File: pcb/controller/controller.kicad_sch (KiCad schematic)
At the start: 1 part, among them U1 XIAO-ESP32-S3-SMD

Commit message: cleaned up
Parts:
- U1: value XIAO-ESP32-S3-SMD -> XIAO-ESP32-C6-SMD
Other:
- note removed: "Target interface"
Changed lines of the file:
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@@
 	(generator_version "9.0")
 	(paper "A4")
-	(text "Target interface"
-		(exclude_from_sim no)
-		(at 248.158 15.24 0)
-		(effects
-			(font
-				(size 1.27 1.27)
-			)
-		)
-	)
 	(no_connect
 		(at 107.95 119.38)
@@
 			)
 		)
-		(property "Value" "XIAO-ESP32-S3-SMD"
+		(property "Value" "XIAO-ESP32-C6-SMD"
 			(at 110.0933 121.92 0)
 			(effects

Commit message: implemented PD, buck and LDO for Power Input
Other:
- sheet Power Input ports: added none; removed GND
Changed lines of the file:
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@@
-	(wire
-		(pts
-			(xy 39.37 43.18) (xy 39.37 45.72)
-		)
-		(stroke
-			(width 0)
-			(type default)
-		)
-	)
 	(wire
 		(pts
@@
 	(wire
 		(pts
-			(xy 39.37 67.31) (xy 39.37 71.12)
-		)
-		(stroke
-			(width 0)
-			(type default)
-		)
-	)
-	(wire
-		(pts
 			(xy 59.69 86.36) (xy 83.82 86.36)
 		)
@@
 		(pts
 			(xy 63.5 99.06) (xy 63.5 90.17)
+		)
+		(stroke
+			(width 0)
+			(type default)
+		)
+	)
+	(wire
+		(pts
+			(xy 41.91 48.26) (xy 41.91 50.8)
 		)
 		(stroke
@@
 	(symbol
 		(lib_id "power:GND")
-		(at 39.37 71.12 0)
-		(unit 1)
-		(exclude_from_sim no)
-		(in_bom yes)
-		(on_board yes)
-		(dnp no)
-		(fields_autoplaced yes)
-		(property "Reference" "#PWR02"
-			(at 39.37 77.47 0)
-			(effects
-				(font
-					(size 1.27 1.27)
-				)
-				(hide yes)
-			)
-		)
-		(property "Value" "GND"
-			(at 39.37 76.2 0)
-			(effects
-				(font
-					(size 1.27 1.27)
-				)
-			)
-		)
-		(property "Footprint" ""
-			(at 39.37 71.12 0)
-			(effects
-				(font
-					(size 1.27 1.27)
-				)
-				(hide yes)
-			)
-		)
-		(property "Datasheet" ""
-			(at 39.37 71.12 0)
-			(effects
-				(font
-					(size 1.27 1.27)
-				)
-				(hide yes)
-			)
-		)
-		(property "Description" "Power symbol creates a global label with name \"GND\" , ground"
-			(at 39.37 71.12 0)
-			(effects
-				(font
-					(size 1.27 1.27)
-				)
-				(hide yes)
-			)
-		)
-		(pin "1"
-		)
-		(instances
-			(project ""
-				(path "/c599d8cf-7937-49be-b4ed-eac09167ead4"
-					(reference "#PWR02")
-					(unit 1)
-				)
-			)
-		)
-	)
-	(symbol
-		(lib_id "power:GND")
 		(at 140.97 90.17 0)
 		(unit 1)
@@
 	(symbol
 		(lib_id "power:+5V")
-		(at 39.37 43.18 0)
+		(at 41.91 48.26 0)
 		(unit 1)
 		(exclude_from_sim no)
@@
 		(fields_autoplaced yes)
 		(property "Reference" "#PWR01"
-			(at 39.37 46.99 0)
+			(at 41.91 52.07 0)
 			(effects
 				(font
@@
 		)
 		(property "Value" "+5V"
-			(at 39.37 38.1 0)
+			(at 41.91 43.18 0)
 			(effects
 				(font
@@
 		)
 		(property "Footprint" ""
-			(at 39.37 43.18 0)
+			(at 41.91 48.26 0)
 			(effects
 				(font
@@
 		)
 		(property "Datasheet" ""
-			(at 39.37 43.18 0)
+			(at 41.91 48.26 0)
 			(effects
 				(font
@@
 		)
 		(property "Description" "Power symbol creates a global label with name \"+5V\""
-			(at 39.37 43.18 0)
+			(at 41.91 48.26 0)
 			(effects
 				(font
@@
 	)
 	(sheet
-		(at 25.4 45.72)
-		(size 26.67 21.59)
+		(at 27.94 50.8)
+		(size 27.94 5.08)
 		(exclude_from_sim no)
 		(in_bom yes)
@@
 		)
 		(property "Sheetname" "Power Input"
-			(at 25.4 45.0084 0)
+			(at 27.94 50.0884 0)
 			(effects
 				(font
@@
 		)
 		(property "Sheetfile" "power_input.kicad_sch"
-			(at 25.4 67.8946 0)
+			(at 27.94 56.4646 0)
 			(effects
 				(font
@@
 			)
 		)
-		(pin "GND" output
-			(at 39.37 67.31 270)
-			(effects
-				(font
-					(size 1.27 1.27)
-				)
-				(justify left)
-			)
-		)
 		(pin "+5V" output
-			(at 39.37 45.72 90)
-			(effects
-				(font
+			(at 41.91 50.8 90)
+			(effects
+				(font

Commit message: impl eFuse
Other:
- sheet Power Input ports: added Imon; removed none
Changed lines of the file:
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@@
+			)
+		)
+		(pin "Imon" output
+			(at 55.88 53.34 0)
+			(effects
+				(font
+					(size 1.27 1.27)
+				)
+				(justify right)
 			)
 		)

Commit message: retraced target pcb
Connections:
- net GND: now also U1.16 (GND), U1.20 (GND)
- net Inputs/RE_B: now also U1.10 (GPIO20_D9_MISO); no longer U1.4 (GPIO21_D3)
- net Inputs/SW1: now also U1.2 (GPIO1_A1_D1); no longer U1.1 (GPIO0_A0_D0)
- net Inputs/SW2: now also U1.3 (GPIO2_A2_D2); no longer U1.2 (GPIO1_A1_D1)
- net Inputs/SW3: now also U1.4 (GPIO21_D3); no longer U1.3 (GPIO2_A2_D2)
- new net Imon: U1.1 (GPIO0_A0_D0)
- no-connect marks 14 -> 11

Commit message: added lcsc numbers to all components and added ESD protection
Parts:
- U1: footprint (none) -> Seeed Studio XIAO Series Library:XIAO-ESP32C6-SMD; now left out of the parts list
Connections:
- net +3.3V: now also U1.24 (3V3_1)
- net Inputs/SW4: now reaches U1.9 (GPIO19_D8_SCK)
- no-connect marks 11 -> 9
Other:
- sheet Inputs ports: added SW4; removed none
- sheet Power Input ports: added none; removed +5V
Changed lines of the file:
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@@
 	(paper "A4")
 	(no_connect
-		(at 119.38 74.93)
-	)
-	(no_connect
-		(at 101.6 119.38)
+		(at 102.87 119.38)
 	)
 	(no_connect
@@
 	)
 	(no_connect
-		(at 127 105.41)
-	)
-	(no_connect
 		(at 92.71 74.93)
 	)
@@
 	(wire
 		(pts
+			(xy 130.81 132.08) (xy 130.81 105.41)
+		)
+		(stroke
+			(width 0)
+			(type default)
+		)
+	)
+	(wire
+		(pts
 			(xy 69.85 99.06) (xy 49.53 99.06)
 		)
@@
 	(wire
 		(pts
-			(xy 137.16 128.27) (xy 69.85 128.27)
-		)
-		(stroke
-			(width 0)
-			(type default)
-		)
-	)
-	(wire
-		(pts
-			(xy 137.16 97.79) (xy 137.16 128.27)
+			(xy 137.16 137.16) (xy 68.58 137.16)
+		)
+		(stroke
+			(width 0)
+			(type default)
+		)
+	)
+	(wire
+		(pts
+			(xy 119.38 72.39) (xy 119.38 74.93)
+		)
+		(stroke
+			(width 0)
+			(type default)
+		)
+	)
+	(wire
+		(pts
+			(xy 73.66 111.76) (xy 73.66 132.08)
+		)
+		(stroke
+			(width 0)
+			(type default)
+		)
+	)
+	(wire
+		(pts
+			(xy 137.16 97.79) (xy 137.16 137.16)
 		)
 		(stroke
@@
 	(wire
 		(pts
-			(xy 49.53 106.68) (xy 72.39 106.68)
-		)
-		(stroke
-			(width 0)
-			(type default)
-		)
-	)
-	(wire
-		(pts
-			(xy 69.85 128.27) (xy 69.85 110.49)
+			(xy 49.53 115.57) (xy 71.12 115.57)
+		)
+		(stroke
+			(width 0)
+			(type default)
+		)
+	)
+	(wire
+		(pts
+			(xy 68.58 137.16) (xy 68.58 119.38)
 		)
 		(stroke
@@
 	(wire
 		(pts
-			(xy 72.39 106.68) (xy 72.39 125.73)
-		)
-		(stroke
-			(width 0)
-			(type default)
-		)
-	)
-	(wire
-		(pts
-			(xy 72.39 125.73) (xy 133.35 125.73)
+			(xy 49.53 111.76) (xy 73.66 111.76)
+		)
+		(stroke
+			(width 0)
+			(type default)
+		)
+	)
+	(wire
+		(pts
+			(xy 71.12 115.57) (xy 71.12 134.62)
+		)
+		(stroke
+			(width 0)
+			(type default)
+		)
+	)
+	(wire
+		(pts
+			(xy 71.12 134.62) (xy 133.35 134.62)
+		)
+		(stroke
+			(width 0)
+			(type default)
+		)
+	)
+	(wire
+		(pts
+			(xy 127 105.41) (xy 130.81 105.41)
 		)
 		(stroke
@@
 	(wire
 		(pts
-			(xy 69.85 110.49) (xy 49.53 110.49)
+			(xy 68.58 119.38) (xy 49.53 119.38)
 		)
 		(stroke
@@
 	(wire
 		(pts
-			(xy 41.91 48.26) (xy 41.91 50.8)
-		)
-		(stroke
-			(width 0)
-			(type default)
-		)
-	)
-	(wire
-		(pts
 			(xy 67.31 90.17) (xy 83.82 90.17)
 		)
@@
 	(wire
 		(pts
-			(xy 133.35 125.73) (xy 133.35 101.6)
+			(xy 73.66 132.08) (xy 130.81 132.08)
+		)
+		(stroke
+			(width 0)
+			(type default)
+		)
+	)
+	(wire
+		(pts
+			(xy 133.35 134.62) (xy 133.35 101.6)
 		)
 		(stroke
@@
 		(unit 1)
 		(exclude_from_sim no)
-		(in_bom yes)
+		(in_bom no)
 		(on_board yes)
 		(dnp no)
@@
 			)
 		)
-		(property "Footprint" ""
+		(property "Footprint" "Seeed Studio XIAO Series Library:XIAO-ESP32C6-SMD"
 			(at 96.52 92.71 0)
 			(effects
@@
 		)
 		(property "Description" ""
+			(at 105.41 97.79 0)
+			(effects
+				(font
+					(size 1.27 1.27)
+				)
+				(hide yes)
+			)
+		)
+		(property "LCSC" ""
 			(at 105.41 97.79 0)
 			(effects
@@
 	)
 	(symbol
-		(lib_id "power:+5V")
-		(at 41.91 48.26 0)
+		(lib_id "power:+3.3V")
+		(at 119.38 72.39 0)
 		(unit 1)
 		(exclude_from_sim no)
@@
 		(on_board yes)
 		(dnp no)
-		(fields_autoplaced yes)
 		(property "Reference" "#PWR01"
-			(at 41.91 52.07 0)
-			(effects
-				(font
-					(size 1.27 1.27)
-				)
-				(hide yes)
-			)
-		)
-		(property "Value" "+5V"
-			(at 41.91 43.18 0)
+			(at 119.38 76.2 0)
+			(effects
+				(font
+					(size 1.27 1.27)
+				)
+				(hide yes)
+			)
+		)
+		(property "Value" "+3.3V"
+			(at 123.444 71.12 0)
 			(effects
 				(font
@@
 		)
 		(property "Footprint" ""
-			(at 41.91 48.26 0)
+			(at 119.38 72.39 0)
 			(effects
 				(font
@@
 		)
 		(property "Datasheet" ""
-			(at 41.91 48.26 0)
-			(effects
-				(font
-					(size 1.27 1.27)
-				)
-				(hide yes)
-			)
-		)
-		(property "Description" "Power symbol creates a global label with name \"+5V\""
-			(at 41.91 48.26 0)
+			(at 119.38 72.39 0)
+			(effects
+				(font
+					(size 1.27 1.27)
+				)
+				(hide yes)
+			)
+		)
+		(property "Description" "Power symbol creates a global label with name \"+3.3V\""
+			(at 119.38 72.39 0)
 			(effects
 				(font
@@
 		)
 		(instances
-			(project ""
+			(project "controller"
 				(path "/c599d8cf-7937-49be-b4ed-eac09167ead4"
 					(reference "#PWR01")
@@
 			)
 		)
-		(pin "+5V" output
-			(at 41.91 50.8 90)
-			(effects
-				(font
-					(size 1.27 1.27)
-				)
-				(justify right)
-			)
-		)
 		(pin "Imon" output
 			(at 55.88 53.34 0)
@@
 	(sheet
 		(at 25.4 93.98)
-		(size 24.13 19.05)
+		(size 24.13 26.67)
 		(exclude_from_sim no)
 		(in_bom yes)
@@
 		)
 		(property "Sheetfile" "inputs.kicad_sch"
-			(at 25.4 113.6146 0)
+			(at 25.4 121.2346 0)
 			(effects
 				(font
@@
 		)
 		(pin "RE_B" output
-			(at 49.53 106.68 0)
+			(at 49.53 115.57 0)
+			(effects
+				(font
+					(size 1.27 1.27)
+				)
+				(justify right)
+			)
+		)
+		(pin "RE_A" output
+			(at 49.53 119.38 0)
+			(effects
+				(font
+					(size 1.27 1.27)
+				)
+				(justify right)
+			)
+		)
+		(pin "SW2" output
+			(at 49.53 99.06 0)
 			(effects
 				(font
@@
 			)
 		)
-		(pin "RE_A" output
-			(at 49.53 110.49 0)
-			(effects
-				(font
-					(size 1.27 1.27)
-				)
-				(justify right)
-			)
-		)
-		(pin "SW2" output
-			(at 49.53 99.06 0)
-			(effects
-				(font
+		(pin "SW4" output
+			(at 49.53 111.76 0)
+			(effects
+				(font

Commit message: did led circle pcb and added 3d models for the controller pcb
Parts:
- U1: footprint Seeed Studio XIAO Series Library:XIAO-ESP32C6-SMD -> external_footprints.petty:XIAO-ESP32C6-SMD
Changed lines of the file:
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@@
 			)
 		)
-		(property "Footprint" "Seeed Studio XIAO Series Library:XIAO-ESP32C6-SMD"
+		(property "Footprint" "external_footprints.petty:XIAO-ESP32C6-SMD"
 			(at 96.52 92.71 0)
 			(effects

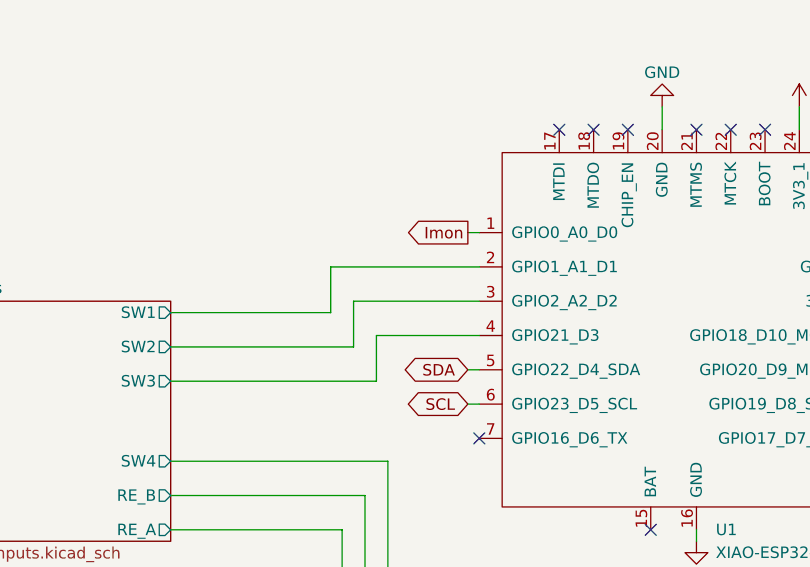
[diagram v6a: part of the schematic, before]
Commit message: traced controller pcb and renamed to Blitzpong
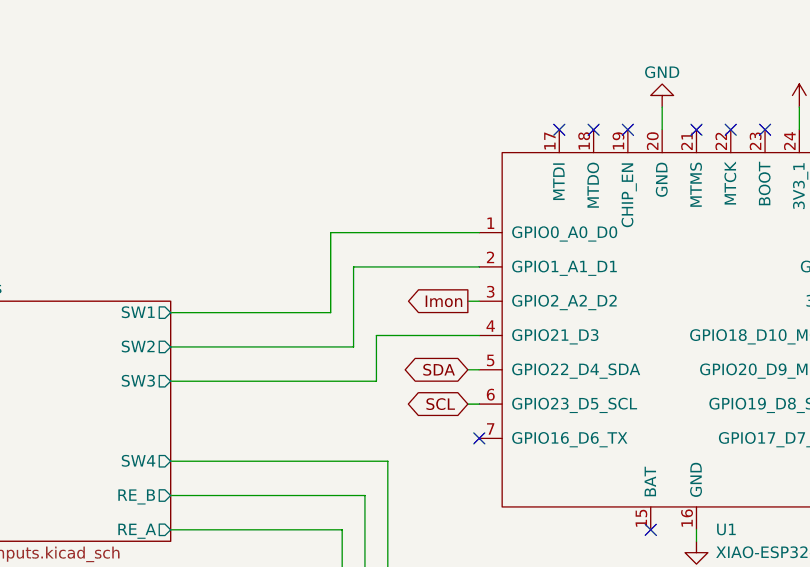
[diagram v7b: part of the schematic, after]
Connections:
- net Imon: now also U1.3 (GPIO2_A2_D2); no longer U1.1 (GPIO0_A0_D0)
- net Inputs/SW1: now also U1.1 (GPIO0_A0_D0); no longer U1.2 (GPIO1_A1_D1)
- net Inputs/SW2: now also U1.2 (GPIO1_A1_D1); no longer U1.3 (GPIO2_A2_D2)
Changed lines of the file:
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@@
+	(wire
+		(pts
+			(xy 82.55 93.98) (xy 83.82 93.98)
+		)
+		(stroke
+			(width 0)
+			(type default)
+		)
+	)
 	(wire
 		(pts
@@
 	(wire
 		(pts
-			(xy 82.55 86.36) (xy 83.82 86.36)
-		)
-		(stroke
-			(width 0)
-			(type default)
-		)
-	)
-	(wire
-		(pts
 			(xy 208.28 85.09) (xy 208.28 88.9)
 		)
@@
 	(wire
 		(pts
-			(xy 69.85 93.98) (xy 69.85 99.06)
-		)
-		(stroke
-			(width 0)
-			(type default)
-		)
-	)
-	(wire
-		(pts
 			(xy 127 101.6) (xy 133.35 101.6)
 		)
@@
 	(wire
 		(pts
-			(xy 67.31 95.25) (xy 67.31 90.17)
+			(xy 67.31 86.36) (xy 67.31 95.25)
 		)
 		(stroke
@@
 	(wire
 		(pts
+			(xy 67.31 86.36) (xy 83.82 86.36)
+		)
+		(stroke
+			(width 0)
+			(type default)
+		)
+	)
+	(wire
+		(pts
 			(xy 82.55 101.6) (xy 83.82 101.6)
 		)
@@
 	(wire
 		(pts
+			(xy 83.82 90.17) (xy 69.85 90.17)
+		)
+		(stroke
+			(width 0)
+			(type default)
+		)
+	)
+	(wire
+		(pts
 			(xy 68.58 119.38) (xy 49.53 119.38)
 		)
@@
 	(wire
 		(pts
-			(xy 83.82 93.98) (xy 69.85 93.98)
-		)
-		(stroke
-			(width 0)
-			(type default)
-		)
-	)
-	(wire
-		(pts
 			(xy 127 97.79) (xy 137.16 97.79)
 		)
@@
 	(wire
 		(pts
-			(xy 67.31 90.17) (xy 83.82 90.17)
+			(xy 69.85 90.17) (xy 69.85 99.06)
 		)
 		(stroke
@@
 	(global_label "Imon"
 		(shape output)
-		(at 82.55 86.36 180)
+		(at 82.55 93.98 180)
 		(fields_autoplaced yes)
 		(effects
@@
 		)
 		(property "Intersheetrefs" "${INTERSHEET_REFS}"
-			(at 74.9687 86.36 0)
+			(at 74.9687 93.98 0)
 			(effects
 				(font

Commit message: Initial commit for v2
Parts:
- removed U1: XIAO-ESP32-C6-SMD, external_footprints.petty:XIAO-ESP32C6-SMD, symbol Seeed_Studio_XIAO_Series:XIAO-ESP32-C6-SMD
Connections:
- no-connect marks 9 -> 0
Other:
- removed sheet Inputs
- removed sheet Power Input
- removed sheet Target Interface
- removed sheet displays
